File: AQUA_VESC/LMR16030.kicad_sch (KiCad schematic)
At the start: 18 parts, among them Q7 AO3400A, U10 LMR16030SDDAR, U11 22uH

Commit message: AQUA VESC仮完成
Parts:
- C61: renamed from C63; value 0.1u -> 100n
- U9: renamed from U10; footprint specific_footprint_library:DDA0008E_L -> Package_SO:SOIC-8-1EP_3.9x4.9mm_P1.27mm_EP2.41x3.3mm_ThermalVias
- renumbered C62 to C60, C64 to C62, C65 to C63, C66 to C64, R70 to R69, R71 to R70, R72 to R71, R73 to R72, R74 to R73, R75 to R74, R76 to R75, R77 to R76, U11 to U10
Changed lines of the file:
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@@
 		(dnp no)
 		(fields_autoplaced yes)
-		(property "Reference" "#PWR099"
+		(property "Reference" "#PWR094"
 			(at 175.26 62.23 0)
 			(effects
@@
 			(project "AQUA_VESC"
 				(path "/8ee9fd02-9bd5-4905-927f-d8ca1179f479/68a50cf0-e0e8-43d7-996b-b4903b1b3f4b"
-					(reference "#PWR099")
+					(reference "#PWR094")
 					(unit 1)
 				)
@@
 		(dnp no)
 		(fields_autoplaced yes)
-		(property "Reference" "U11"
+		(property "Reference" "U10"
 			(at 147.32 45.72 0)
 			(effects
@@
 			(project ""
 				(path "/8ee9fd02-9bd5-4905-927f-d8ca1179f479/68a50cf0-e0e8-43d7-996b-b4903b1b3f4b"
-					(reference "U11")
+					(reference "U10")
 					(unit 1)
 				)
@@
 		(dnp no)
 		(fields_autoplaced yes)
-		(property "Reference" "#PWR093"
+		(property "Reference" "#PWR087"
 			(at 102.87 76.2 0)
 			(effects
@@
 			(project "AQUA_VESC"
 				(path "/8ee9fd02-9bd5-4905-927f-d8ca1179f479/68a50cf0-e0e8-43d7-996b-b4903b1b3f4b"
-					(reference "#PWR093")
+					(reference "#PWR087")
 					(unit 1)
 				)
@@
 		(dnp no)
 		(fields_autoplaced yes)
-		(property "Reference" "R75"
+		(property "Reference" "R74"
 			(at 105.41 74.9299 0)
 			(effects
@@
 			(project "AQUA_VESC"
 				(path "/8ee9fd02-9bd5-4905-927f-d8ca1179f479/68a50cf0-e0e8-43d7-996b-b4903b1b3f4b"
-					(reference "R75")
+					(reference "R74")
 					(unit 1)
 				)
@@
 		(dnp no)
 		(fields_autoplaced yes)
-		(property "Reference" "C64"
+		(property "Reference" "C62"
 			(at 158.75 52.0699 0)
 			(effects
@@
 			(project ""
 				(path "/8ee9fd02-9bd5-4905-927f-d8ca1179f479/68a50cf0-e0e8-43d7-996b-b4903b1b3f4b"
-					(reference "C64")
+					(reference "C62")
 					(unit 1)
 				)
@@
 		(on_board yes)
 		(dnp no)
-		(property "Reference" "R72"
+		(property "Reference" "R71"
 			(at 86.614 57.658 90)
 			(effects
@@
 			(project "AQUA_VESC"
 				(path "/8ee9fd02-9bd5-4905-927f-d8ca1179f479/68a50cf0-e0e8-43d7-996b-b4903b1b3f4b"
-					(reference "R72")
+					(reference "R71")
 					(unit 1)
 				)
@@
 		(dnp no)
 		(fields_autoplaced yes)
-		(property "Reference" "C66"
+		(property "Reference" "C64"
 			(at 179.07 52.0699 0)
 			(effects
@@
 			(project "AQUA_VESC"
 				(path "/8ee9fd02-9bd5-4905-927f-d8ca1179f479/68a50cf0-e0e8-43d7-996b-b4903b1b3f4b"
-					(reference "C66")
+					(reference "C64")
 					(unit 1)
 				)
@@
 		(dnp no)
 		(fields_autoplaced yes)
-		(property "Reference" "#PWR095"
+		(property "Reference" "#PWR089"
 			(at 137.16 74.93 0)
 			(effects
@@
 			(project ""
 				(path "/8ee9fd02-9bd5-4905-927f-d8ca1179f479/68a50cf0-e0e8-43d7-996b-b4903b1b3f4b"
-					(reference "#PWR095")
+					(reference "#PWR089")
 					(unit 1)
 				)
@@
 		(dnp no)
 		(fields_autoplaced yes)
-		(property "Reference" "C62"
+		(property "Reference" "C60"
 			(at 92.71 31.7499 0)
 			(effects
@@
 			(project "AQUA_VESC"
 				(path "/8ee9fd02-9bd5-4905-927f-d8ca1179f479/68a50cf0-e0e8-43d7-996b-b4903b1b3f4b"
-					(reference "C62")
+					(reference "C60")
 					(unit 1)
 				)
@@
 		(dnp no)
 		(fields_autoplaced yes)
-		(property "Reference" "R71"
+		(property "Reference" "R70"
 			(at 69.85 53.3399 0)
 			(effects
@@
 			(project "AQUA_VESC"
 				(path "/8ee9fd02-9bd5-4905-927f-d8ca1179f479/68a50cf0-e0e8-43d7-996b-b4903b1b3f4b"
-					(reference "R71")
+					(reference "R70")
 					(unit 1)
 				)
@@
 		(dnp no)
 		(fields_autoplaced yes)
-		(property "Reference" "#PWR089"
+		(property "Reference" "#PWR083"
 			(at 67.31 71.12 0)
 			(effects
@@
 			(project "AQUA_VESC"
 				(path "/8ee9fd02-9bd5-4905-927f-d8ca1179f479/68a50cf0-e0e8-43d7-996b-b4903b1b3f4b"
-					(reference "#PWR089")
+					(reference "#PWR083")
 					(unit 1)
 				)
@@
 		(on_board yes)
 		(dnp no)
-		(property "Reference" "R76"
+		(property "Reference" "R75"
 			(at 156.21 67.3099 0)
 			(effects
@@
 			(project "AQUA_VESC"
 				(path "/8ee9fd02-9bd5-4905-927f-d8ca1179f479/68a50cf0-e0e8-43d7-996b-b4903b1b3f4b"
-					(reference "R76")
+					(reference "R75")
 					(unit 1)
 				)
@@
 		(dnp no)
 		(fields_autoplaced yes)
-		(property "Reference" "U10"
+		(property "Reference" "U9"
 			(at 119.38 31.75 0)
 			(effects
@@
 			)
 		)
-		(property "Footprint" "specific_footprint_library:DDA0008E_L"
+		(property "Footprint" "Package_SO:SOIC-8-1EP_3.9x4.9mm_P1.27mm_EP2.41x3.3mm_ThermalVias"
 			(at 119.38 52.07 0)
 			(effects
@@
 			(project ""
 				(path "/8ee9fd02-9bd5-4905-927f-d8ca1179f479/68a50cf0-e0e8-43d7-996b-b4903b1b3f4b"
-					(reference "U10")
+					(reference "U9")
 					(unit 1)
 				)
@@
 		(on_board yes)
 		(dnp no)
-		(property "Reference" "#PWR094"
+		(property "Reference" "#PWR088"
 			(at 102.87 106.68 0)
 			(effects
@@
 			(project "AQUA_VESC"
 				(path "/8ee9fd02-9bd5-4905-927f-d8ca1179f479/68a50cf0-e0e8-43d7-996b-b4903b1b3f4b"
-					(reference "#PWR094")
+					(reference "#PWR088")
 					(unit 1)
 				)
@@
 		(on_board yes)
 		(dnp no)
-		(property "Reference" "R73"
+		(property "Reference" "R72"
 			(at 93.726 51.308 90)
 			(effects
@@
 			(project ""
 				(path "/8ee9fd02-9bd5-4905-927f-d8ca1179f479/68a50cf0-e0e8-43d7-996b-b4903b1b3f4b"
-					(reference "R73")
+					(reference "R72")
 					(unit 1)
 				)
@@
 		(dnp no)
 		(fields_autoplaced yes)
-		(property "Reference" "R70"
+		(property "Reference" "R69"
 			(at 69.85 36.8299 0)
 			(effects
@@
 			(project "AQUA_VESC"
 				(path "/8ee9fd02-9bd5-4905-927f-d8ca1179f479/68a50cf0-e0e8-43d7-996b-b4903b1b3f4b"
-					(reference "R70")
+					(reference "R69")
 					(unit 1)
 				)
@@
 		(dnp no)
 		(fields_autoplaced yes)
-		(property "Reference" "#PWR096"
+		(property "Reference" "#PWR091"
 			(at 153.67 90.17 0)
 			(effects
@@
 			(project "AQUA_VESC"
 				(path "/8ee9fd02-9bd5-4905-927f-d8ca1179f479/68a50cf0-e0e8-43d7-996b-b4903b1b3f4b"
-					(reference "#PWR096")
+					(reference "#PWR091")
 					(unit 1)
 				)
@@
 		(dnp no)
 		(fields_autoplaced yes)
-		(property "Reference" "#PWR098"
+		(property "Reference" "#PWR093"
 			(at 165.1 62.23 0)
 			(effects
@@
 			(project "AQUA_VESC"
 				(path "/8ee9fd02-9bd5-4905-927f-d8ca1179f479/68a50cf0-e0e8-43d7-996b-b4903b1b3f4b"
-					(reference "#PWR098")
+					(reference "#PWR093")
 					(unit 1)
 				)
@@
 		(on_board yes)
 		(dnp no)
-		(property "Reference" "C63"
+		(property "Reference" "C61"
 			(at 141.224 37.592 0)
 			(effects
@@
 			)
 		)
-		(property "Value" "0.1u"
+		(property "Value" "100n"
 			(at 141.224 39.878 0)
 			(effects
@@
 			(project ""
 				(path "/8ee9fd02-9bd5-4905-927f-d8ca1179f479/68a50cf0-e0e8-43d7-996b-b4903b1b3f4b"
-					(reference "C63")
+					(reference "C61")
 					(unit 1)
 				)
@@
 		(dnp no)
 		(fields_autoplaced yes)
-		(property "Reference" "#PWR091"
+		(property "Reference" "#PWR085"
 			(at 81.28 66.04 0)
 			(effects
@@
 			(project ""
 				(path "/8ee9fd02-9bd5-4905-927f-d8ca1179f479/68a50cf0-e0e8-43d7-996b-b4903b1b3f4b"
-					(reference "#PWR091")
+					(reference "#PWR085")
 					(unit 1)
 				)
@@
 		(dnp no)
 		(fields_autoplaced yes)
-		(property "Reference" "#PWR092"
+		(property "Reference" "#PWR086"
 			(at 88.9 41.91 0)
 			(effects
@@
 			(project "AQUA_VESC"
 				(path "/8ee9fd02-9bd5-4905-927f-d8ca1179f479/68a50cf0-e0e8-43d7-996b-b4903b1b3f4b"
-					(reference "#PWR092")
+					(reference "#PWR086")
 					(unit 1)
 				)
@@
 		(dnp no)
 		(fields_autoplaced yes)
-		(property "Reference" "#PWR090"
+		(property "Reference" "#PWR084"
 			(at 77.47 71.12 0)
 			(effects
@@
 			(project "AQUA_VESC"
 				(path "/8ee9fd02-9bd5-4905-927f-d8ca1179f479/68a50cf0-e0e8-43d7-996b-b4903b1b3f4b"
-					(reference "#PWR090")
+					(reference "#PWR084")
 					(unit 1)
 				)
@@
 		(dnp no)
 		(fields_autoplaced yes)
-		(property "Reference" "#PWR0109"
+		(property "Reference" "#PWR090"
 			(at 140.97 62.23 0)
 			(effects
@@
 			(project "AQUA_VESC"
 				(path "/8ee9fd02-9bd5-4905-927f-d8ca1179f479/68a50cf0-e0e8-43d7-996b-b4903b1b3f4b"
-					(reference "#PWR0109")
+					(reference "#PWR090")
 					(unit 1)
 				)
@@
 		(dnp no)
 		(fields_autoplaced yes)
-		(property "Reference" "#PWR097"
+		(property "Reference" "#PWR092"
 			(at 154.94 62.23 0)
 			(effects
@@
 			(project "AQUA_VESC"
 				(path "/8ee9fd02-9bd5-4905-927f-d8ca1179f479/68a50cf0-e0e8-43d7-996b-b4903b1b3f4b"
-					(reference "#PWR097")
+					(reference "#PWR092")
 					(unit 1)
 				)
@@
 		(dnp no)
 		(fields_autoplaced yes)
-		(property "Reference" "R77"
+		(property "Reference" "R76"
 			(at 156.21 77.4699 0)
 			(effects
@@
 			(project "AQUA_VESC"
 				(path "/8ee9fd02-9bd5-4905-927f-d8ca1179f479/68a50cf0-e0e8-43d7-996b-b4903b1b3f4b"
-					(reference "R77")
+					(reference "R76")
 					(unit 1)
 				)
@@
 		(dnp no)
 		(fields_autoplaced yes)
-		(property "Reference" "#PWR0100"
+		(property "Reference" "#PWR095"
 			(at 180.34 45.72 0)
 			(effects
@@
 			(project "AQUA_VESC"
 				(path "/8ee9fd02-9bd5-4905-927f-d8ca1179f479/68a50cf0-e0e8-43d7-996b-b4903b1b3f4b"
-					(reference "#PWR0100")
+					(reference "#PWR095")
 					(unit 1)
 				)
@@
 		(on_board yes)
 		(dnp no)
-		(property "Reference" "R74"
+		(property "Reference" "R73"
 			(at 96.774 57.658 90)
 			(effects
@@
 			(project "AQUA_VESC"
 				(path "/8ee9fd02-9bd5-4905-927f-d8ca1179f479/68a50cf0-e0e8-43d7-996b-b4903b1b3f4b"
-					(reference "R74")
+					(reference "R73")
 					(unit 1)
 				)
@@
 		(dnp no)
 		(fields_autoplaced yes)
-		(property "Reference" "C65"
+		(property "Reference" "C63"
 			(at 168.91 52.0699 0)
 			(effects
@@
 			(project "AQUA_VESC"
 				(path "/8ee9fd02-9bd5-4905-927f-d8ca1179f479/68a50cf0-e0e8-43d7-996b-b4903b1b3f4b"
-					(reference "C65")
-					(unit 1)
-				)
+					(reference "C63")
+					(unit 1)
+				)

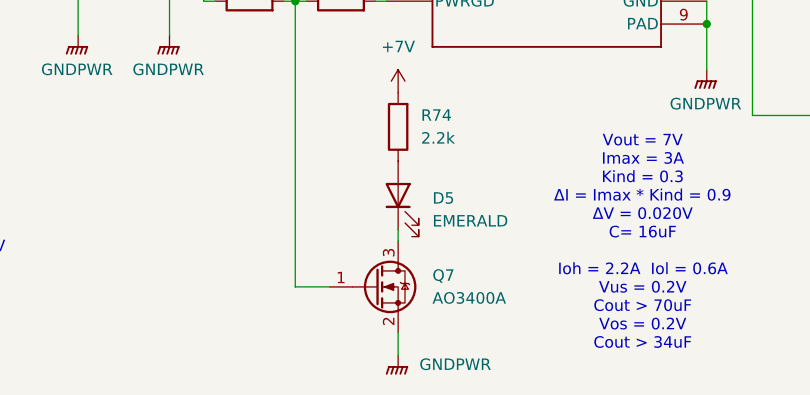
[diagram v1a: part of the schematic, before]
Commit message: AQUA_VESC REV01作成
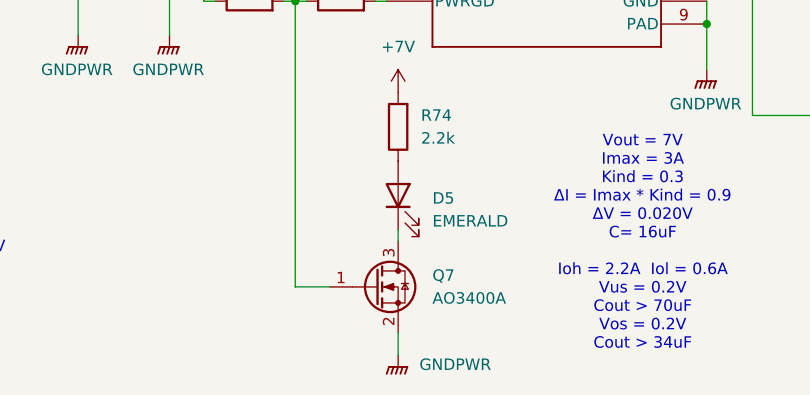
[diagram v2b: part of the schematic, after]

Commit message: 制御基板REV01完成
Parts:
- renumbered C60 to C62, C61 to C63, C62 to C64, C63 to C65, C64 to C66
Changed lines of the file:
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@@
 		(dnp no)
 		(fields_autoplaced yes)
-		(property "Reference" "#PWR094"
+		(property "Reference" "#PWR095"
 			(at 175.26 62.23 0)
 			(effects
@@
 			(project "AQUA_VESC"
 				(path "/8ee9fd02-9bd5-4905-927f-d8ca1179f479/68a50cf0-e0e8-43d7-996b-b4903b1b3f4b"
-					(reference "#PWR094")
+					(reference "#PWR095")
 					(unit 1)
 				)
@@
 		(dnp no)
 		(fields_autoplaced yes)
-		(property "Reference" "#PWR087"
+		(property "Reference" "#PWR088"
 			(at 102.87 76.2 0)
 			(effects
@@
 			(project "AQUA_VESC"
 				(path "/8ee9fd02-9bd5-4905-927f-d8ca1179f479/68a50cf0-e0e8-43d7-996b-b4903b1b3f4b"
-					(reference "#PWR087")
+					(reference "#PWR088")
 					(unit 1)
 				)
@@
 		(dnp no)
 		(fields_autoplaced yes)
-		(property "Reference" "C62"
+		(property "Reference" "C64"
 			(at 158.75 52.0699 0)
 			(effects
@@
 			(project ""
 				(path "/8ee9fd02-9bd5-4905-927f-d8ca1179f479/68a50cf0-e0e8-43d7-996b-b4903b1b3f4b"
-					(reference "C62")
+					(reference "C64")
 					(unit 1)
 				)
@@
 		(dnp no)
 		(fields_autoplaced yes)
-		(property "Reference" "C64"
+		(property "Reference" "C66"
 			(at 179.07 52.0699 0)
 			(effects
@@
 			(project "AQUA_VESC"
 				(path "/8ee9fd02-9bd5-4905-927f-d8ca1179f479/68a50cf0-e0e8-43d7-996b-b4903b1b3f4b"
-					(reference "C64")
+					(reference "C66")
 					(unit 1)
 				)
@@
 		(dnp no)
 		(fields_autoplaced yes)
-		(property "Reference" "#PWR089"
+		(property "Reference" "#PWR090"
 			(at 137.16 74.93 0)
 			(effects
@@
 			(project ""
 				(path "/8ee9fd02-9bd5-4905-927f-d8ca1179f479/68a50cf0-e0e8-43d7-996b-b4903b1b3f4b"
-					(reference "#PWR089")
+					(reference "#PWR090")
 					(unit 1)
 				)
@@
 		(dnp no)
 		(fields_autoplaced yes)
-		(property "Reference" "C60"
+		(property "Reference" "C62"
 			(at 92.71 31.7499 0)
 			(effects
@@
 			(project "AQUA_VESC"
 				(path "/8ee9fd02-9bd5-4905-927f-d8ca1179f479/68a50cf0-e0e8-43d7-996b-b4903b1b3f4b"
-					(reference "C60")
+					(reference "C62")
 					(unit 1)
 				)
@@
 		(dnp no)
 		(fields_autoplaced yes)
-		(property "Reference" "#PWR083"
+		(property "Reference" "#PWR084"
 			(at 67.31 71.12 0)
 			(effects
@@
 			(project "AQUA_VESC"
 				(path "/8ee9fd02-9bd5-4905-927f-d8ca1179f479/68a50cf0-e0e8-43d7-996b-b4903b1b3f4b"
-					(reference "#PWR083")
+					(reference "#PWR084")
 					(unit 1)
 				)
@@
 		(on_board yes)
 		(dnp no)
-		(property "Reference" "#PWR088"
+		(property "Reference" "#PWR089"
 			(at 102.87 106.68 0)
 			(effects
@@
 			(project "AQUA_VESC"
 				(path "/8ee9fd02-9bd5-4905-927f-d8ca1179f479/68a50cf0-e0e8-43d7-996b-b4903b1b3f4b"
-					(reference "#PWR088")
+					(reference "#PWR089")
 					(unit 1)
 				)
@@
 		(dnp no)
 		(fields_autoplaced yes)
-		(property "Reference" "#PWR091"
+		(property "Reference" "#PWR092"
 			(at 153.67 90.17 0)
 			(effects
@@
 			(project "AQUA_VESC"
 				(path "/8ee9fd02-9bd5-4905-927f-d8ca1179f479/68a50cf0-e0e8-43d7-996b-b4903b1b3f4b"
-					(reference "#PWR091")
+					(reference "#PWR092")
 					(unit 1)
 				)
@@
 		(dnp no)
 		(fields_autoplaced yes)
-		(property "Reference" "#PWR093"
+		(property "Reference" "#PWR094"
 			(at 165.1 62.23 0)
 			(effects
@@
 			(project "AQUA_VESC"
 				(path "/8ee9fd02-9bd5-4905-927f-d8ca1179f479/68a50cf0-e0e8-43d7-996b-b4903b1b3f4b"
-					(reference "#PWR093")
+					(reference "#PWR094")
 					(unit 1)
 				)
@@
 		(on_board yes)
 		(dnp no)
-		(property "Reference" "C61"
+		(property "Reference" "C63"
 			(at 141.224 37.592 0)
 			(effects
@@
 			(project ""
 				(path "/8ee9fd02-9bd5-4905-927f-d8ca1179f479/68a50cf0-e0e8-43d7-996b-b4903b1b3f4b"
-					(reference "C61")
+					(reference "C63")
 					(unit 1)
 				)
@@
 		(dnp no)
 		(fields_autoplaced yes)
-		(property "Reference" "#PWR085"
+		(property "Reference" "#PWR086"
 			(at 81.28 66.04 0)
 			(effects
@@
 			(project ""
 				(path "/8ee9fd02-9bd5-4905-927f-d8ca1179f479/68a50cf0-e0e8-43d7-996b-b4903b1b3f4b"
-					(reference "#PWR085")
+					(reference "#PWR086")
 					(unit 1)
 				)
@@
 		(dnp no)
 		(fields_autoplaced yes)
-		(property "Reference" "#PWR086"
+		(property "Reference" "#PWR087"
 			(at 88.9 41.91 0)
 			(effects
@@
 			(project "AQUA_VESC"
 				(path "/8ee9fd02-9bd5-4905-927f-d8ca1179f479/68a50cf0-e0e8-43d7-996b-b4903b1b3f4b"
-					(reference "#PWR086")
+					(reference "#PWR087")
 					(unit 1)
 				)
@@
 		(dnp no)
 		(fields_autoplaced yes)
-		(property "Reference" "#PWR084"
+		(property "Reference" "#PWR085"
 			(at 77.47 71.12 0)
 			(effects
@@
 			(project "AQUA_VESC"
 				(path "/8ee9fd02-9bd5-4905-927f-d8ca1179f479/68a50cf0-e0e8-43d7-996b-b4903b1b3f4b"
-					(reference "#PWR084")
+					(reference "#PWR085")
 					(unit 1)
 				)
@@
 		(dnp no)
 		(fields_autoplaced yes)
-		(property "Reference" "#PWR090"
+		(property "Reference" "#PWR091"
 			(at 140.97 62.23 0)
 			(effects
@@
 			(project "AQUA_VESC"
 				(path "/8ee9fd02-9bd5-4905-927f-d8ca1179f479/68a50cf0-e0e8-43d7-996b-b4903b1b3f4b"
-					(reference "#PWR090")
+					(reference "#PWR091")
 					(unit 1)
 				)
@@
 		(dnp no)
 		(fields_autoplaced yes)
-		(property "Reference" "#PWR092"
+		(property "Reference" "#PWR093"
 			(at 154.94 62.23 0)
 			(effects
@@
 			(project "AQUA_VESC"
 				(path "/8ee9fd02-9bd5-4905-927f-d8ca1179f479/68a50cf0-e0e8-43d7-996b-b4903b1b3f4b"
-					(reference "#PWR092")
+					(reference "#PWR093")
 					(unit 1)
 				)
@@
 		(dnp no)
 		(fields_autoplaced yes)
-		(property "Reference" "#PWR095"
+		(property "Reference" "#PWR096"
 			(at 180.34 45.72 0)
 			(effects
@@
 			(project "AQUA_VESC"
 				(path "/8ee9fd02-9bd5-4905-927f-d8ca1179f479/68a50cf0-e0e8-43d7-996b-b4903b1b3f4b"
-					(reference "#PWR095")
+					(reference "#PWR096")
 					(unit 1)
 				)
@@
 		(dnp no)
 		(fields_autoplaced yes)
-		(property "Reference" "C63"
+		(property "Reference" "C65"
 			(at 168.91 52.0699 0)
 			(effects
@@
 			(project "AQUA_VESC"
 				(path "/8ee9fd02-9bd5-4905-927f-d8ca1179f479/68a50cf0-e0e8-43d7-996b-b4903b1b3f4b"
-					(reference "C63")
-					(unit 1)
-				)
+					(reference "C65")
+					(unit 1)
+				)
